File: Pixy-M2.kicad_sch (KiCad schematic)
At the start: 78 parts, among them J1 USB_C_Receptacle_USB2.0_14P, J10 SM09B-SRSS-TB, J11 SM06B-SRSS-TB, J4 SM06B-SRSS-TB, J5 SM06B-SRSS-TB, J6 SM06B-SRSS-TB, J7 SM06B-SRSS-TB, J8 S6B-PH-K, J9 S6B-PH-K, Q1 AO4407A, SW1 SW_Push, SW2 SW_Push, SW3 JS102011SAQN, U1 ESP32-S3-WROOM-1-N16, U2 USBLC6-2SC6, U3 AP63203WU, U4 DRV8231ADSG, U5 DRV8231ADSG

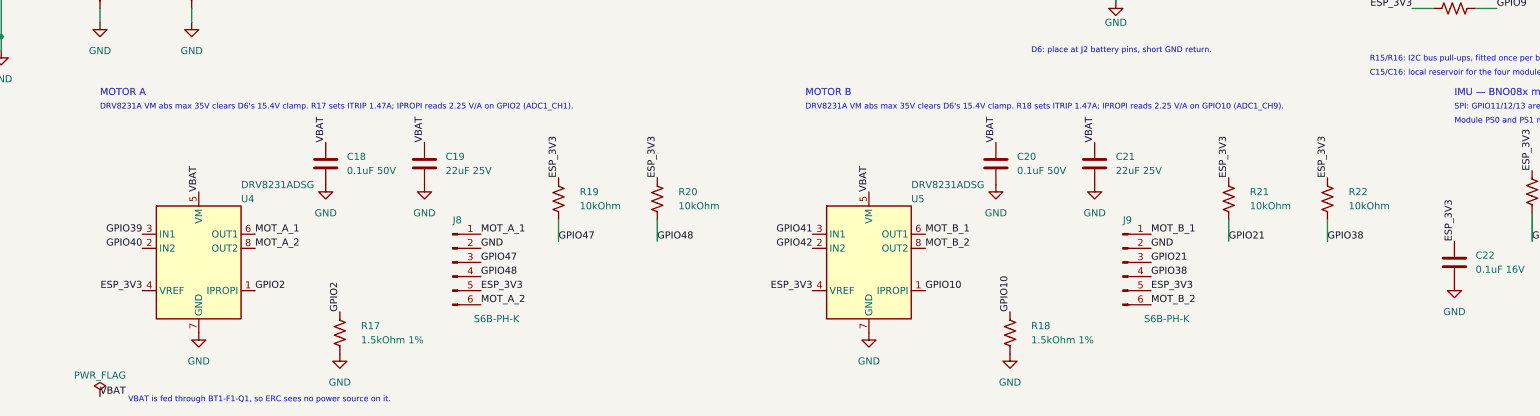
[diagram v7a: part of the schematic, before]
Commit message: layout: move J8/J9 to JST SH in the Pololu encoder pin order
J8/J9 were 2.0 mm JST PH wired M1 GND A B VCC M2. The Pololu 12 CPR encoder
on the chosen gearmotors (#5153-#5165) is a 1.0 mm JST SH header wired
GND B A VCC M2 M1, so a 1:1 cable would have put motor voltage on the encoder
supply. Both connectors are now SM06B-SRSS-TB (the J4-J7 part) in Pololu's
order, MP pads to GND, and take Pololu's straight SH-SH cable (#4765-#4769).

SH contacts and that cable are rated 1 A, so R17/R18 go 1.5 -> 2.2 kOhm:
ITRIP 1.47 -> 1.00 A, IPROPI 2.25 -> 3.3 V/A (ADC clips at ~0.94 A).

Schematic: J8/J9 become Conn_01x06_MountingPin (mirrored, so the pin ends stay
on the existing labels); labels re-pinned; MP wired to GND; R17/R18 values and
the two sheet notes updated. Netlist diff shows only those changes; ERC 0.

Board: new last routing stage, tools/autoroute/pololu_conn.py, run by
rework.py after issue8.py. It swaps the footprints for SH clones of J4 (same
rotations, inside the old courtyards), rips the motor trunks back to the
driver escapes, drops other-net copper under the new pad rows (GPIO2/39/40
ran between the old through-hole pins), prunes what that leaves dangling near
the connectors, then re-routes: paired 0.8 mm trunks with 0.6 mm fan-in stubs,
0.2 mm signal reconnections, plane stitches, and U4's VREF feed, whose only 3V3
path under the In2 VBAT island was the old J8 through-hole pin.

                           before        after
  motor A loop area        103.3 mm2     23.9 mm2
  motor B loop area        83.4 mm2      9.8 mm2
  IPROPI to motor copper   0.29 mm       0.53 mm
  vias                     243           253
Other guarded clearances unchanged. Only 13 nets' tracks/vias changed.
DRC: 0 violations, 0 unconnected, 0 parity. Aperture audit passes.

loop.py now finds each pair's connector end by net, so it measures boards
from before and after the re-pin alike.

Co-Authored-By: Claude Opus 5.5 <noreply@anthropic.com>
Claude-Session: https://claude.ai/cod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
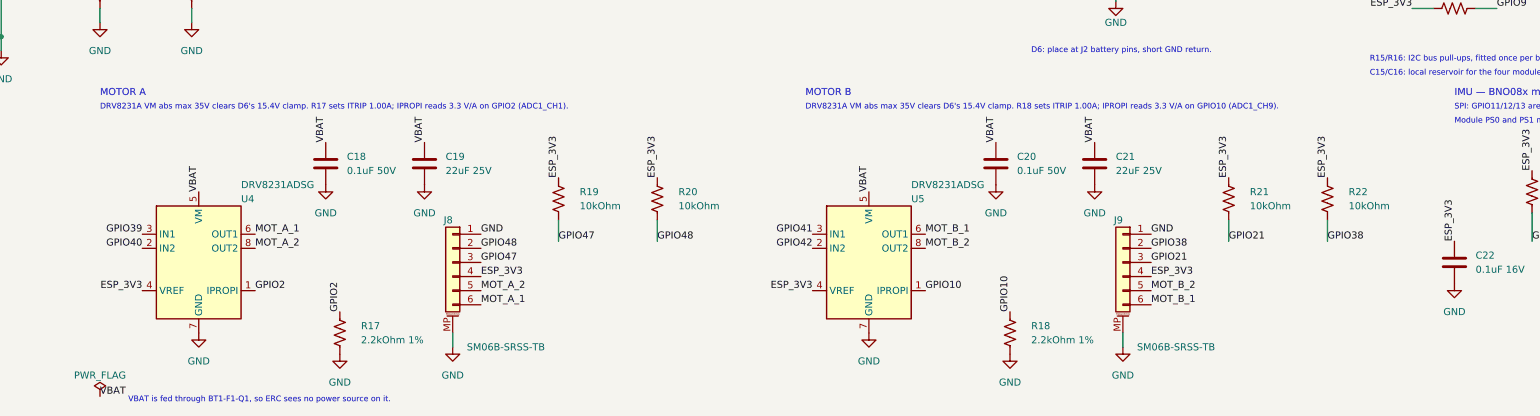
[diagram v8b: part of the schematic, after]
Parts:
- J8, J9: value S6B-PH-K -> SM06B-SRSS-TB; footprint Connector_JST:JST_PH_S6B-PH-K_1x06_P2.00mm_Horizontal -> Connector_JST:JST_SH_SM06B-SRSS-TB_1x06-1MP_P1.00mm_Horizontal; symbol Connector:Conn_01x06_Pin -> Connector_Generic_MountingPin:Conn_01x06_MountingPin; MPN (none) -> SM06B-SRSS-TB(LF)(SN)
- R17, R18: value 1.5kOhm 1% -> 2.2kOhm 1%
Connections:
- net ESP_3V3: now also J8.4 (Pin_4), J9.4 (Pin_4); no longer J8.5 (Pin_5), J9.5 (Pin_5)
- net GND: now also J8.1 (Pin_1), J8.MP (MountPin), J9.1 (Pin_1), J9.MP (MountPin); no longer J8.2 (Pin_2), J9.2 (Pin_2)
- net GPIO38: now also J9.2 (Pin_2); no longer J9.4 (Pin_4)
- net GPIO48: now also J8.2 (Pin_2); no longer J8.4 (Pin_4)
- net MOT_A_1: now also J8.6 (Pin_6); no longer J8.1 (Pin_1)
- net MOT_A_2: now also J8.5 (Pin_5); no longer J8.6 (Pin_6)
- net MOT_B_1: now also J9.6 (Pin_6); no longer J9.1 (Pin_1)
- net MOT_B_2: now also J9.5 (Pin_5); no longer J9.6 (Pin_6)
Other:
- note added: "DRV8231A VM abs max 35V clears D6's 15.4V clamp. R17 sets ITRIP 1.00A; IPROPI reads 3.3 V/A on GPIO2 (ADC1_CH1)."
- note added: "DRV8231A VM abs max 35V clears D6's 15.4V clamp. R18 sets ITRIP 1.00A; IPROPI reads 3.3 V/A on GPIO10 (ADC1_CH9)."
- note removed: "DRV8231A VM abs max 35V clears D6's 15.4V clamp. R17 sets ITRIP 1.47A; IPROPI reads 2.25 V/A on GPIO2 (ADC1_CH1)."
- note removed: "DRV8231A VM abs max 35V clears D6's 15.4V clamp. R18 sets ITRIP 1.47A; IPROPI reads 2.25 V/A on GPIO10 (ADC1_CH9)."
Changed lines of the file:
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@@
 			)
 		)
-		(property "Value" "1.5kOhm 1%"
+		(property "Value" "2.2kOhm 1%"
 			(at 110.49 242.57 0)
 			(show_name no)
@@
 			)
 		)
-		(property "Description" "RIPROPI. ITRIP = VREF/(AIPROPI*R) = 3.3/(1500u*1500) = 1.47A; sense scale 2.25 V/A."
+		(property "Description" "RIPROPI. ITRIP = VREF/(AIPROPI*R) = 3.3/(1500u*2200) = 1.00A (JST SH contact rating 1A); sense scale 3.3 V/A."
 			(at 106.68 241.3 0)
 			(hide yes)
@@
 	)
 	(symbol
-		(lib_id "Connector:Conn_01x06_Pin")
+		(lib_id "Connector_Generic_MountingPin:Conn_01x06_MountingPin")
 		(at 127.0 228.6 0)
+		(mirror y)
 		(unit 1)
 		(body_style 1)
@@
 			)
 		)
-		(property "Value" "S6B-PH-K"
-			(at 130.81 238.76 0)
+		(property "Value" "SM06B-SRSS-TB"
+			(at 129.54 243.84 0)
+			(show_name no)
+			(do_not_autoplace no)
+			(effects
+				(font
+					(size 1.27 1.27)
+				)
+				(justify right)
+			)
+		)
+		(property "Footprint" "Connector_JST:JST_SH_SM06B-SRSS-TB_1x06-1MP_P1.00mm_Horizontal"
+			(at 127.0 228.6 0)
+			(hide yes)
 			(show_name no)
 			(do_not_autoplace no)
@@
 					(size 1.27 1.27)
 				)
-				(justify left)
 			)
 		)
-		(property "Footprint" "Connector_JST:JST_PH_S6B-PH-K_1x06_P2.00mm_Horizontal"
+		(property "Datasheet" "https://www.jst-mfg.com/product/pdf/eng/eSH.pdf"
 			(at 127.0 228.6 0)
 			(hide yes)
@@
 			)
 		)
-		(property "Datasheet" "https://www.jst-mfg.com/product/pdf/eng/ePH.pdf"
+		(property "Description" "Motor A + encoder (Pololu micro metal gearmotor, 12 CPR encoder). Pololu pin order: 1=GND 2=OUTB 3=OUTA 4=VCC 5=M2 6=M1. Straight SH-SH cable (Pololu #4766-4769)."
 			(at 127.0 228.6 0)
 			(hide yes)
@@
 			)
 		)
-		(property "Description" "Motor A + encoder. Pin order mirrors the encoder module: 1=M1 2=GND 3=OUTA 4=OUTB 5=VCC 6=M2."
+		(property "MPN" "SM06B-SRSS-TB(LF)(SN)"
 			(at 127.0 228.6 0)
 			(hide yes)
@@
 		(pin "6"
 		)
+		(pin "MP"
+		)
 		(instances
 			(project "Pixy-M2"
@@
 		)
 	)
-	(label "MOT_A_1"
+	(label "GND"
 		(at 132.08 223.51999999999998 0)
 		(effects
@@
 		)
 	)
-	(label "GND"
+	(label "GPIO48"
 		(at 132.08 226.05999999999997 0)
 		(effects
@@
 		)
 	)
-	(label "GPIO48"
+	(label "ESP_3V3"
 		(at 132.08 231.14 0)
 		(effects
@@
 		)
 	)
-	(label "ESP_3V3"
+	(label "MOT_A_2"
 		(at 132.08 233.67999999999998 0)
 		(effects
@@
 		)
 	)
-	(label "MOT_A_2"
+	(label "MOT_A_1"
 		(at 132.08 236.21999999999997 0)
 		(effects
@@
 		)
 	)
-	(text "DRV8231A VM abs max 35V clears D6's 15.4V clamp. R17 sets ITRIP 1.47A; IPROPI reads 2.25 V/A on GPIO2 (ADC1_CH1)."
+	(text "DRV8231A VM abs max 35V clears D6's 15.4V clamp. R17 sets ITRIP 1.00A; IPROPI reads 3.3 V/A on GPIO2 (ADC1_CH1)."
 		(at 63.5 200.66 0)
 		(effects
@@
 			)
 		)
-		(property "Value" "1.5kOhm 1%"
+		(property "Value" "2.2kOhm 1%"
 			(at 231.14 242.57 0)
 			(show_name no)
@@
 			)
 		)
-		(property "Description" "RIPROPI. ITRIP = VREF/(AIPROPI*R) = 3.3/(1500u*1500) = 1.47A; sense scale 2.25 V/A."
+		(property "Description" "RIPROPI. ITRIP = VREF/(AIPROPI*R) = 3.3/(1500u*2200) = 1.00A (JST SH contact rating 1A); sense scale 3.3 V/A."
 			(at 227.33 241.3 0)
 			(hide yes)
@@
 	)
 	(symbol
-		(lib_id "Connector:Conn_01x06_Pin")
+		(lib_id "Connector_Generic_MountingPin:Conn_01x06_MountingPin")
 		(at 247.65 228.6 0)
+		(mirror y)
 		(unit 1)
 		(body_style 1)
@@
 			)
 		)
-		(property "Value" "S6B-PH-K"
-			(at 251.46 238.76 0)
+		(property "Value" "SM06B-SRSS-TB"
+			(at 250.19 243.84 0)
 			(show_name no)
 			(do_not_autoplace no)
@@
 					(size 1.27 1.27)
 				)
-				(justify left)
+				(justify right)
 			)
 		)
-		(property "Footprint" "Connector_JST:JST_PH_S6B-PH-K_1x06_P2.00mm_Horizontal"
+		(property "Footprint" "Connector_JST:JST_SH_SM06B-SRSS-TB_1x06-1MP_P1.00mm_Horizontal"
 			(at 247.65 228.6 0)
 			(hide yes)
@@
 			)
 		)
-		(property "Datasheet" "https://www.jst-mfg.com/product/pdf/eng/ePH.pdf"
+		(property "Datasheet" "https://www.jst-mfg.com/product/pdf/eng/eSH.pdf"
 			(at 247.65 228.6 0)
 			(hide yes)
@@
 			)
 		)
-		(property "Description" "Motor B + encoder. Pin order mirrors the encoder module: 1=M1 2=GND 3=OUTA 4=OUTB 5=VCC 6=M2."
+		(property "Description" "Motor B + encoder (Pololu micro metal gearmotor, 12 CPR encoder). Pololu pin order: 1=GND 2=OUTB 3=OUTA 4=VCC 5=M2 6=M1. Straight SH-SH cable (Pololu #4766-4769)."
+			(at 247.65 228.6 0)
+			(hide yes)
+			(show_name no)
+			(do_not_autoplace no)
+			(effects
+				(font
+					(size 1.27 1.27)
+				)
+			)
+		)
+		(property "MPN" "SM06B-SRSS-TB(LF)(SN)"
 			(at 247.65 228.6 0)
 			(hide yes)
@@
 		(pin "6"
 		)
+		(pin "MP"
+		)
 		(instances
 			(project "Pixy-M2"
@@
 		)
 	)
-	(label "MOT_B_1"
+	(label "GND"
 		(at 252.73000000000002 223.51999999999998 0)
 		(effects
@@
 		)
 	)
-	(label "GND"
+	(label "GPIO38"
 		(at 252.73000000000002 226.05999999999997 0)
 		(effects
@@
 		)
 	)
-	(label "GPIO38"
+	(label "ESP_3V3"
 		(at 252.73000000000002 231.14 0)
 		(effects
@@
 		)
 	)
-	(label "ESP_3V3"
+	(label "MOT_B_2"
 		(at 252.73000000000002 233.67999999999998 0)
 		(effects
@@
 		)
 	)
-	(label "MOT_B_2"
+	(label "MOT_B_1"
 		(at 252.73000000000002 236.21999999999997 0)
 		(effects
@@
 		)
 	)
-	(text "DRV8231A VM abs max 35V clears D6's 15.4V clamp. R18 sets ITRIP 1.47A; IPROPI reads 2.25 V/A on GPIO10 (ADC1_CH9)."
+	(text "DRV8231A VM abs max 35V clears D6's 15.4V clamp. R18 sets ITRIP 1.00A; IPROPI reads 3.3 V/A on GPIO10 (ADC1_CH9)."
 		(at 190.5 200.66 0)
 		(effects
@@
 		)
 	)
+	(wire
+		(pts
+			(xy 127.0 241.3) (xy 127.0 243.84)
+		)
+		(stroke
+			(width 0)
+			(type default)
+		)
+	)
+	(symbol
+		(lib_id "power:GND")
+		(at 127.0 243.84 0)
+		(unit 1)
+		(body_style 1)
+		(exclude_from_sim no)
+		(in_bom yes)
+		(on_board yes)
+		(in_pos_files yes)
+		(dnp no)
+		(property "Reference" "#PWR043"
+			(at 127.0 250.19 0)
+			(hide yes)
+			(show_name no)
+			(do_not_autoplace no)
+			(effects
+				(font
+					(size 1.27 1.27)
+				)
+			)
+		)
+		(property "Value" "GND"
+			(at 127.0 248.92 0)
+			(show_name no)
+			(do_not_autoplace no)
+			(effects
+				(font
+					(size 1.27 1.27)
+				)
+			)
+		)
+		(property "Footprint" ""
+			(at 127.0 243.84 0)
+			(hide yes)
+			(show_name no)
+			(do_not_autoplace no)
+			(effects
+				(font
+					(size 1.27 1.27)
+				)
+			)
+		)
+		(property "Datasheet" ""
+			(at 127.0 243.84 0)
+			(hide yes)
+			(show_name no)
+			(do_not_autoplace no)
+			(effects
+				(font
+					(size 1.27 1.27)
+				)
+			)
+		)
+		(property "Description" ""
+			(at 127.0 243.84 0)
+			(hide yes)
+			(show_name no)
+			(do_not_autoplace no)
+			(effects
+				(font
+					(size 1.27 1.27)
+				)
+			)
+		)
+		(pin "1"
+		)
+		(instances
+			(project "Pixy-M2"
+				(path "/fefb2c5c-cd05-4562-bf27-32a51f81fd04"
+					(reference "#PWR043")
+					(unit 1)
+				)
+			)
+		)
+	)
+	(wire
+		(pts
+			(xy 247.65 241.3) (xy 247.65 243.84)
+		)
+		(stroke
+			(width 0)
+			(type default)
+		)
+	)
+	(symbol
+		(lib_id "power:GND")
+		(at 247.65 243.84 0)
+		(unit 1)
+		(body_style 1)
+		(exclude_from_sim no)
+		(in_bom yes)
+		(on_board yes)
+		(in_pos_files yes)
+		(dnp no)
+		(property "Reference" "#PWR044"
+			(at 247.65 250.19 0)
+			(hide yes)
+			(show_name no)
+			(do_not_autoplace no)
+			(effects
+				(font
+					(size 1.27 1.27)
+				)
+			)
+		)
+		(property "Value" "GND"
+			(at 247.65 248.92 0)
+			(show_name no)
+			(do_not_autoplace no)
+			(effects
+				(font
+					(size 1.27 1.27)
+				)
+			)
+		)
+		(property "Footprint" ""
+			(at 247.65 243.84 0)
+			(hide yes)
+			(show_name no)
+			(do_not_autoplace no)
+			(effects
+				(font
+					(size 1.27 1.27)
+				)
+			)
+		)
+		(property "Datasheet" ""
+			(at 247.65 243.84 0)
+			(hide yes)
+			(show_name no)
+			(do_not_autoplace no)
+			(effects
+				(font
+					(size 1.27 1.27)
+				)
+			)
+		)
+		(property "Description" ""
+			(at 247.65 243.84 0)
+			(hide yes)
+			(show_name no)
+			(do_not_autoplace no)
+			(effects
+				(font
+					(size 1.27 1.27)
+				)
+			)
+		)
+		(pin "1"
+		)
+		(instances
+			(project "Pixy-M2"
+				(path "/fefb2c5c-cd05-4562-bf27-32a51f81fd04"
+					(reference "#PWR044")
+					(unit 1)
+				)
+			)
+		)
+	)
